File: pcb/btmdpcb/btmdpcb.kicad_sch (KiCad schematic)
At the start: 27 parts, among them Q1 BSD235C, Q2 2N7000, Q3 2N7000, Q4 2N7000, Q5 BSD235C

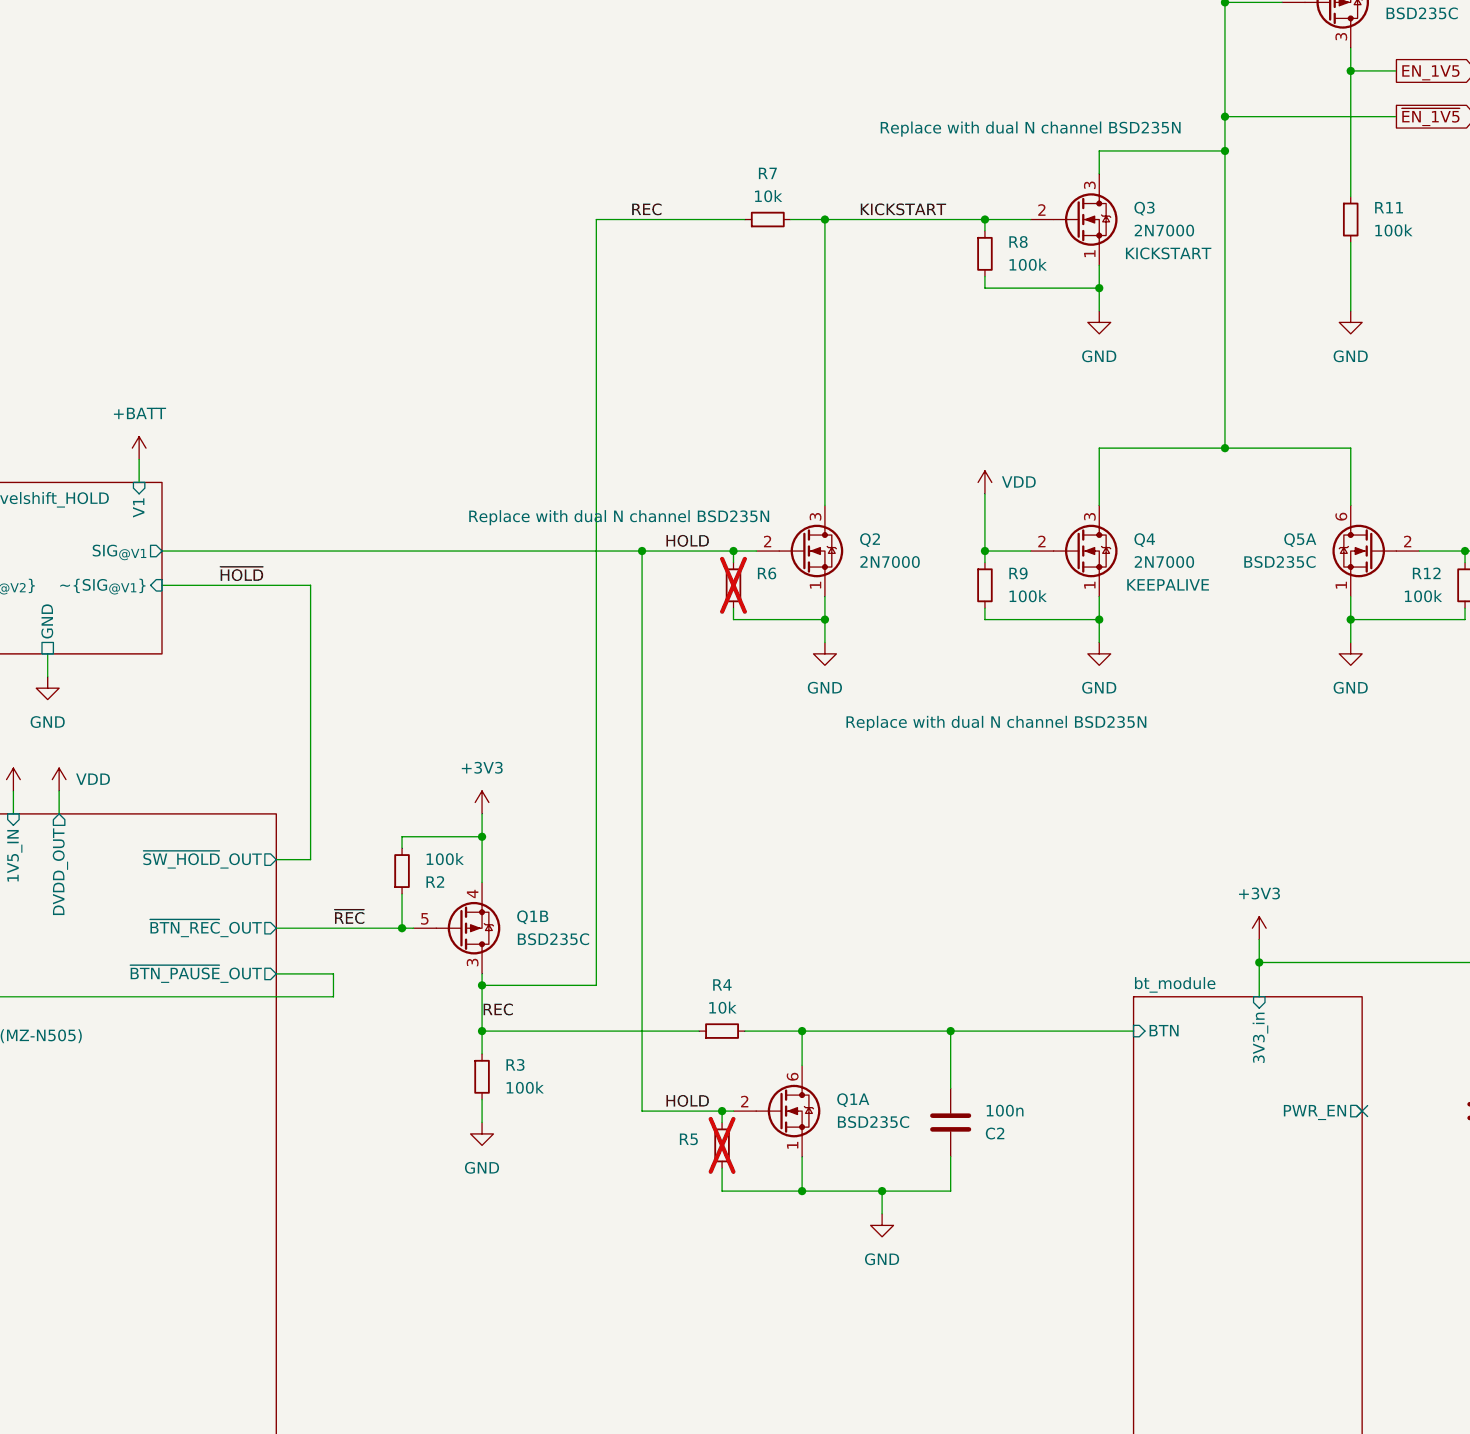
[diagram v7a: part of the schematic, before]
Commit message: Simplify circuit; reduce transistor count
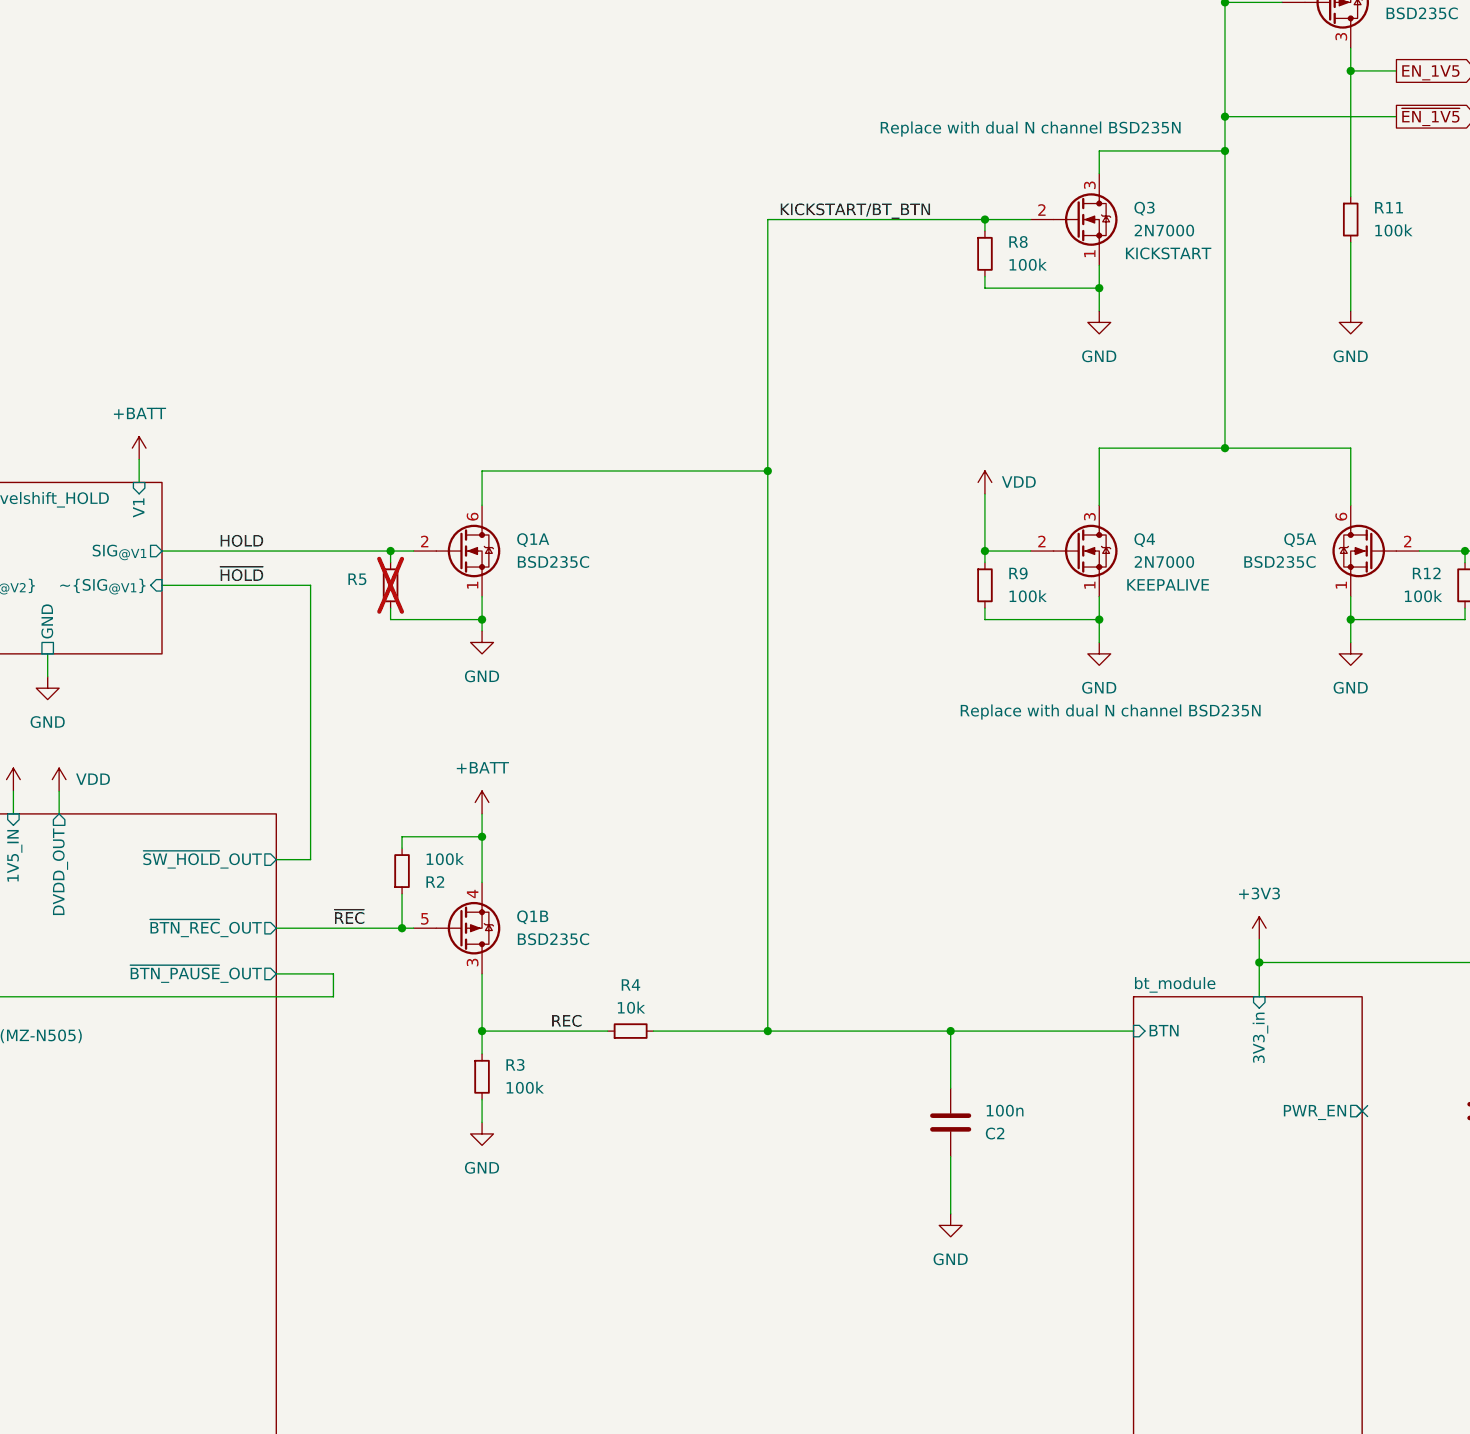
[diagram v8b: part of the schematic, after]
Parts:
- removed Q2: 2N7000, Package_TO_SOT_THT:TO-92_Inline, symbol Transistor_FET:2N7000
- removed R6: ~, symbol Device:R_Small
- removed R7: 10k, symbol Device:R_Small
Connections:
- net bt_module/BTN is gone; now on net KICKSTART/BT_BTN: C2.2, Q1.6 (DN), R4.2
- net +3V3: no longer Q1.4 (SP), R2.2
- net +BATT: now also Q1.4 (SP), R2.2
- net KICKSTART renamed KICKSTART/BT_BTN
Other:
- moved on the sheet: Q1A, R4, R5
